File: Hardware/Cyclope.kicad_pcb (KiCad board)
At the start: 2 copper layers, 100 x 84 mm, 81 parts, among them J1 M20-9762042, J2 Motor_2, J3 Motor_1, J4 Front, J5 Front, J8 FTDI, M1 FS5113R, M2 FS5113R, Q1 DMG3414U, Q2 DMG2301L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

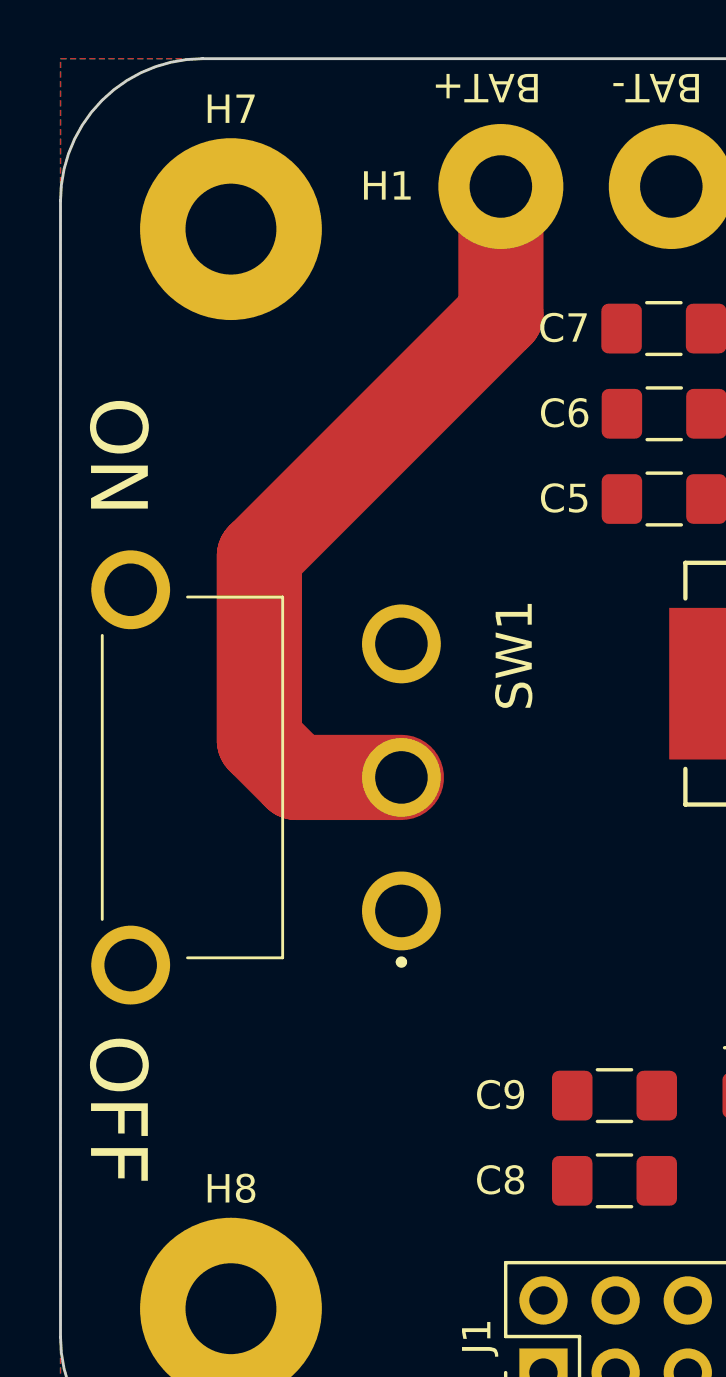
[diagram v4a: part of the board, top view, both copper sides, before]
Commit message: [Hardware] Changed power switch pins order to ease routing.
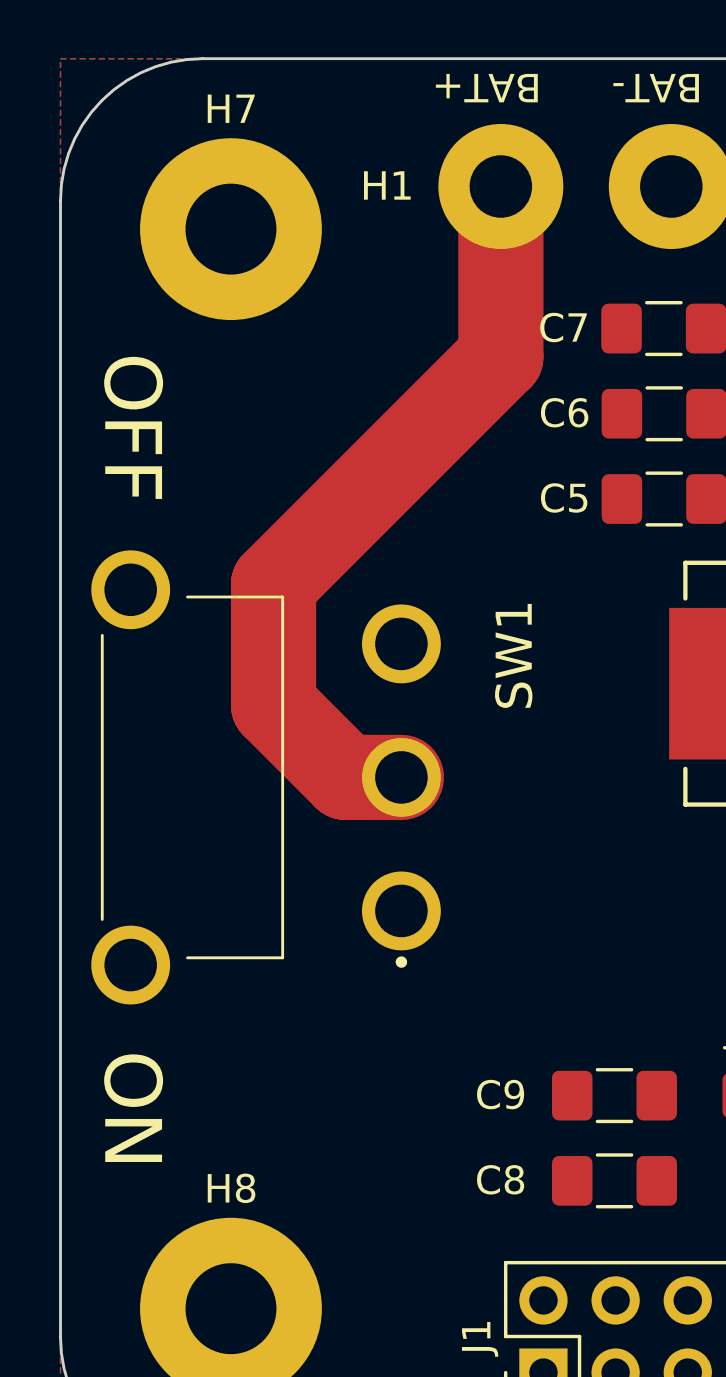
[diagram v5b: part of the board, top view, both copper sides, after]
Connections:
- SW1 pad 1: Net-(SW1-Pad1) -> BATTERY+
- SW1 pad 3: BATTERY+ -> Net-(SW1-Pad3)
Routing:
- net Net-(H1-Pad1): track 28.6 -> 27.1 mm

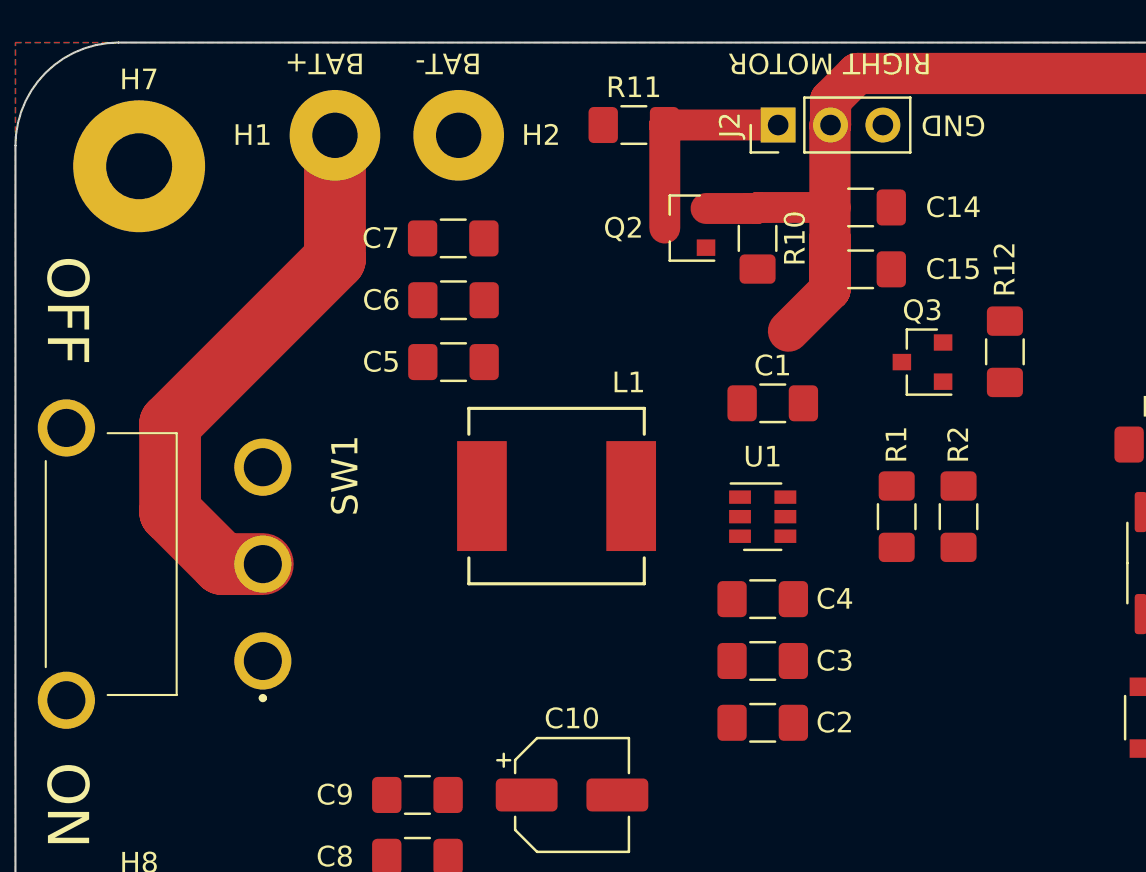
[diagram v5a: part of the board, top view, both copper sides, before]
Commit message: [Hardware] Routed motherboard DC/DC.
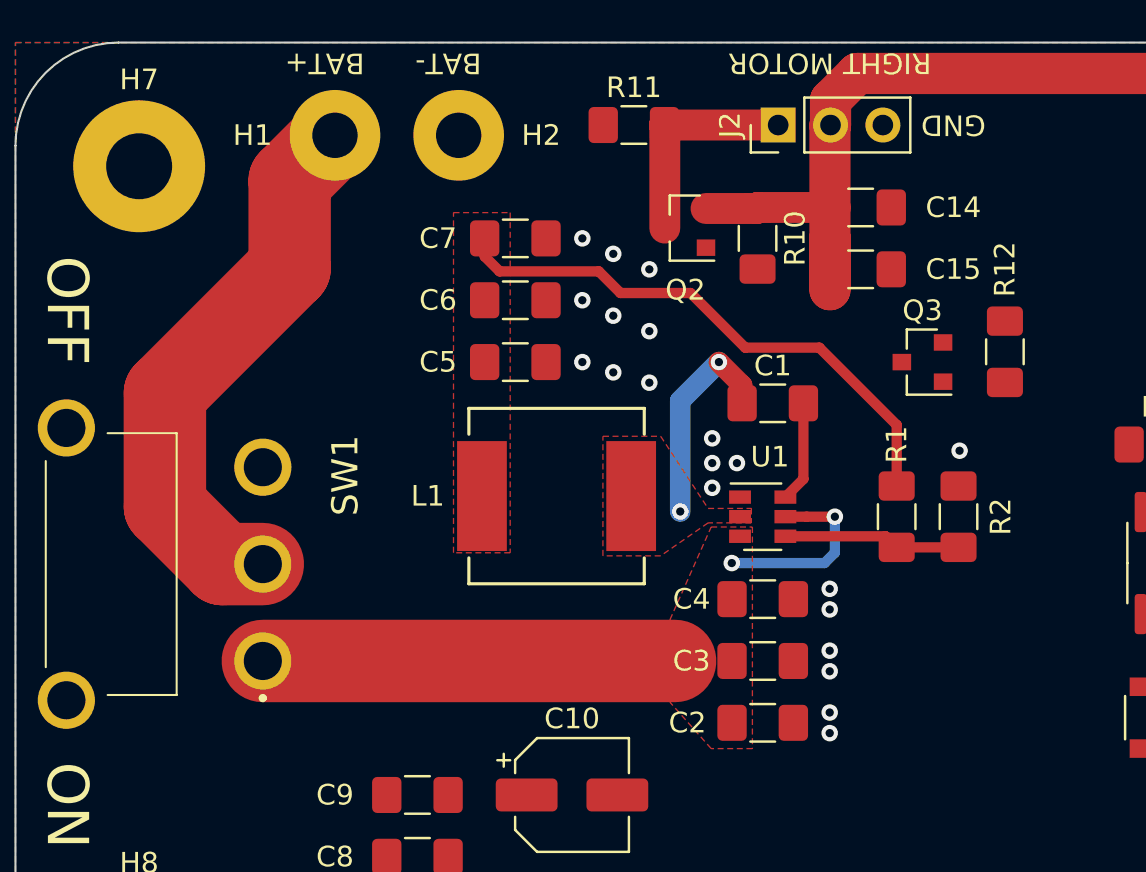
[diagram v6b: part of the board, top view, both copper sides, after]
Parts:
- moved C7 3.01 mm to (81.8, 69.5), turned to 180 degrees
- moved C5 3.00 mm to (81.8, 75.5), turned to 180 degrees
- moved C6 3.00 mm to (81.8, 72.5), turned to 180 degrees
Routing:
- net BATTERY+: track 0.00 -> 29.4 mm, vias 0 -> 2
- net +5V: track 76.6 -> 101.0 mm
- net Net-(C1-Pad1): track 0.00 -> 10.5 mm, vias 0 -> 2
- net Net-(R1-Pad2): track 0.00 -> 8.62 mm
- net Net-(C1-Pad2): track 0.00 -> 4.91 mm
- net GND: vias 0 -> 20
- added copper zone on F.Cu, net +5V
- added copper zone on F.Cu, net BATTERY+
- added copper zone on F.Cu, net Net-(C1-Pad1)

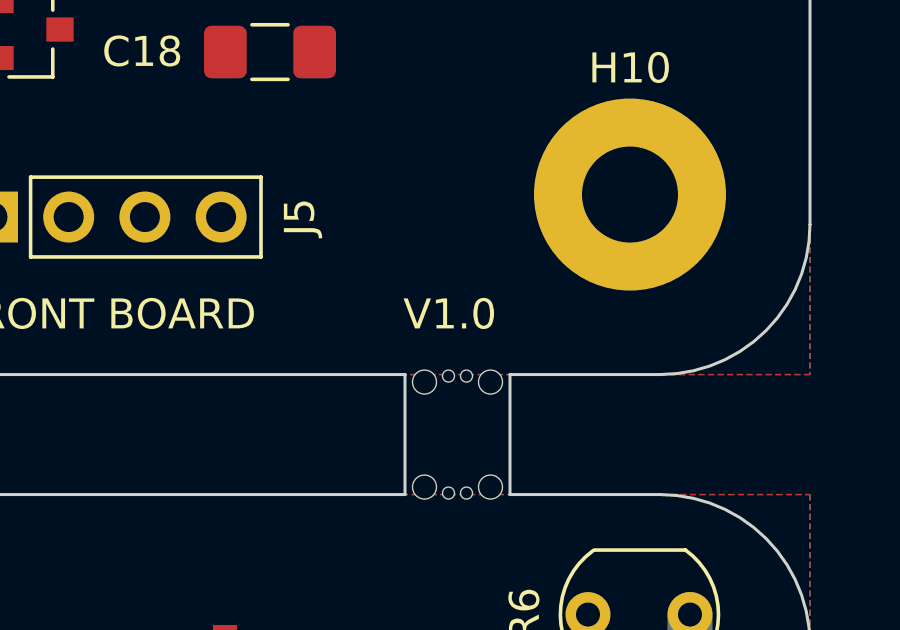
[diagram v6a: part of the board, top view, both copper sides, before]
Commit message: [Hardware] Added date marking to PCBs.
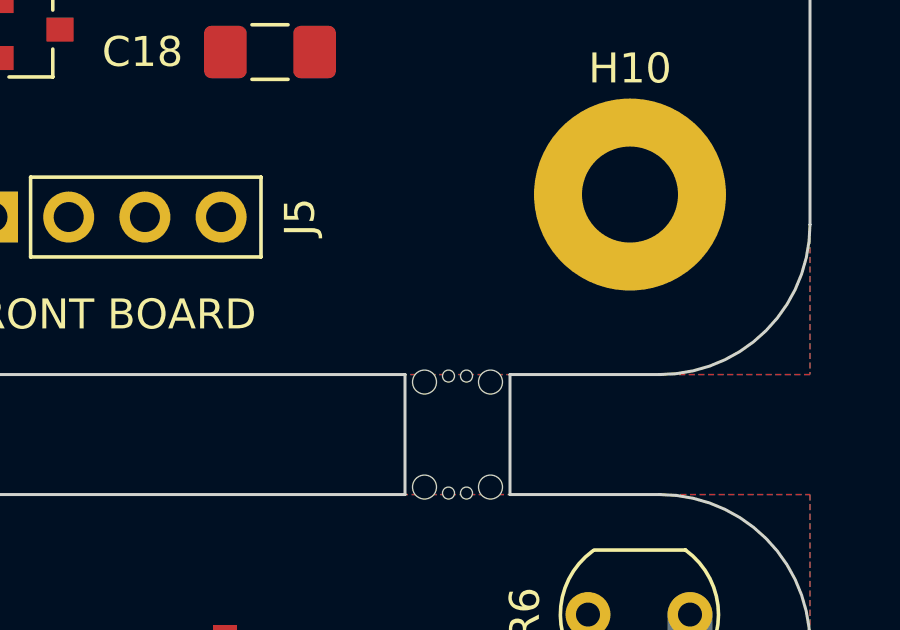
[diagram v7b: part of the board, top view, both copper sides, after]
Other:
- board text added: "14/08/2020"
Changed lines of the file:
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@@
   (general
     (thickness 1.6)
-    (drawings 64)
+    (drawings 66)
     (tracks 125)
     (zones 0)
@@
     )
   )
+  (gr_text 14/08/2020 (at 147.25 83.5 90) (layer F.Mask)
+    (effects (font (size 1 1) (thickness 0.15)))
+  )
+  (gr_text V1.0 (at 147.25 75.25 90) (layer F.Mask)
+    (effects (font (size 1 1) (thickness 0.15)))
+  )
+  (gr_text 14/08/2020 (at 133.25 142) (layer B.Mask)
+    (effects (font (size 1 1) (thickness 0.15)) (justify mirror))
+  )
   (gr_text GND (at 103 64 180) (layer F.SilkS)
     (effects (font (size 1 1) (thickness 0.15)))
@@
     (effects (font (size 1 1) (thickness 0.15)))
   )
-  (gr_text V1.0 (at 145.5 108) (layer F.SilkS)
-    (effects (font (size 1 1) (thickness 0.15)))
-  )
-  (gr_text V1.0 (at 141.5 142) (layer B.SilkS)
+  (gr_text V1.0 (at 141.5 142) (layer B.Mask)
     (effects (font (size 1 1) (thickness 0.15)) (justify mirror))
   )

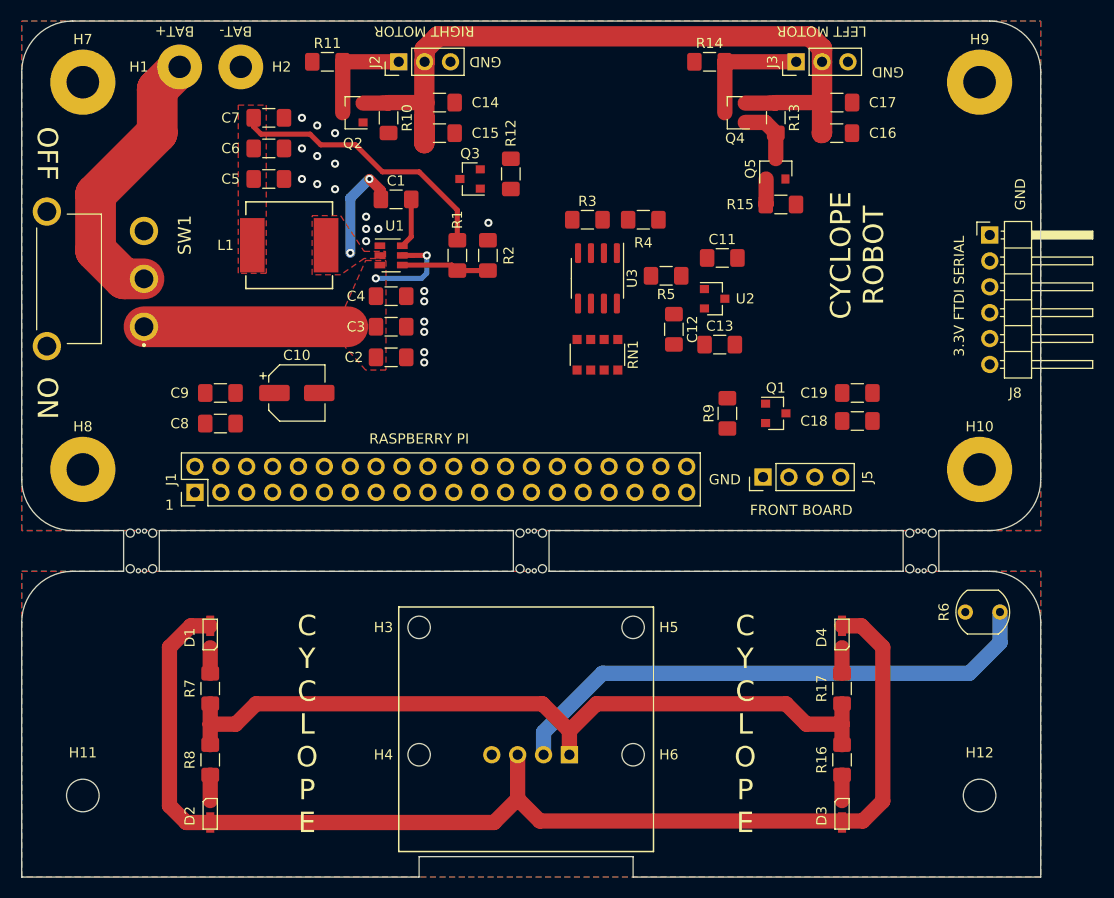
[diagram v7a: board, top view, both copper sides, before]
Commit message: [Hardware] Routed part of ADC, routed Raspberry Pi power supply.
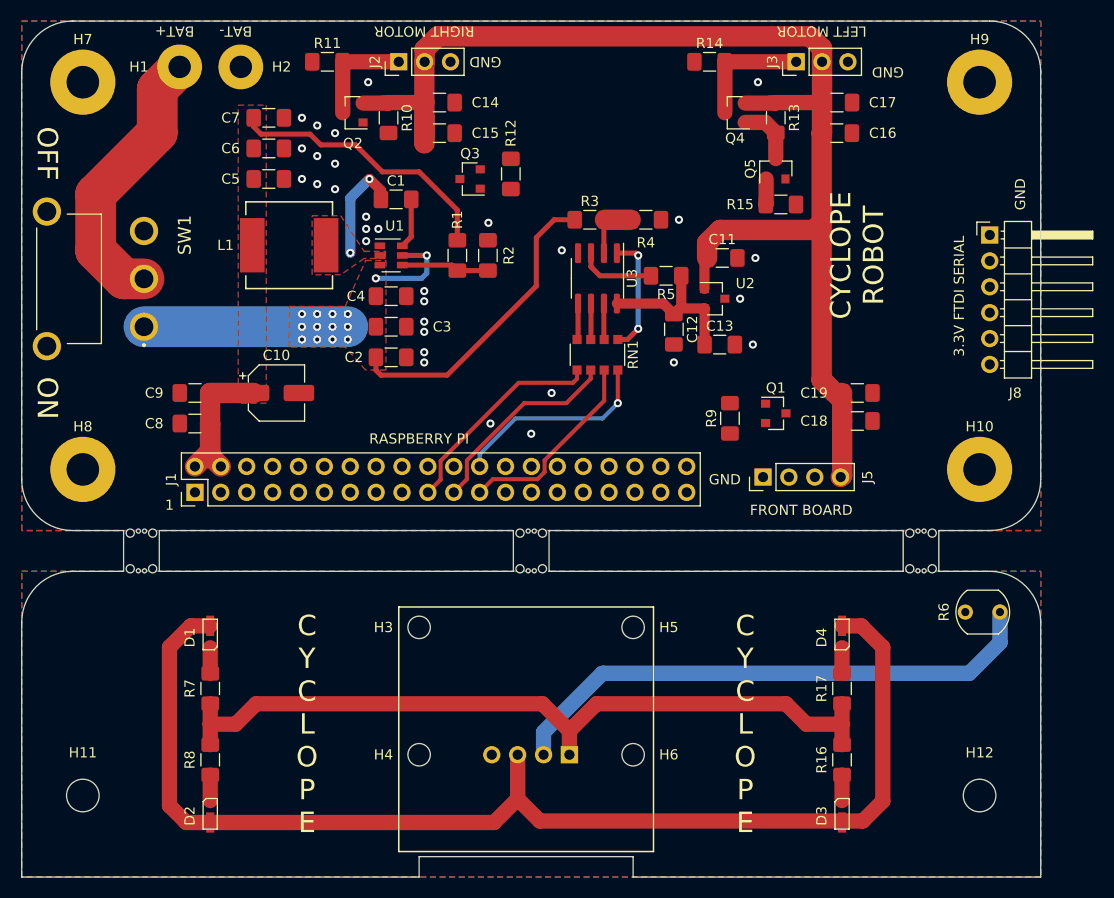
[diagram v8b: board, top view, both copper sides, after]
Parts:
- moved C8 2.50 mm to (74.5, 99.5)
- moved C9 2.50 mm to (74.5, 96.5)
- moved C10 2.00 mm to (82.5, 96.5)
- moved R9 0.55 mm to (127.0, 99.0)
- moved R4 0.25 mm to (118.8, 79.5)
- moved R3 0.24 mm to (113.2, 79.5)
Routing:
- net +5V: track 101.0 -> 171.7 mm
- net BATTERY+: track 29.4 -> 59.4 mm, vias 2 -> 14
- net ADC_SPI_MOSI: track 0.00 -> 21.2 mm
- net ADC_SPI_CS: track 0.00 -> 20.1 mm, vias 0 -> 1
- net ADC_SPI_MISO: track 0.00 -> 20.0 mm
- net ADC_SPI_SCK: track 0.00 -> 19.6 mm
- net +3.3VA: track 0.00 -> 16.9 mm
- net Net-(RN1-Pad1): track 0.00 -> 11.8 mm, vias 0 -> 2
- net FRONT_BOARD_LDR: track 0.00 -> 7.59 mm
- net Net-(R3-Pad2): track 0.00 -> 5.84 mm
- net Net-(RN1-Pad4): track 0.00 -> 3.56 mm
- net Net-(RN1-Pad3): track 0.00 -> 3.54 mm
- net Net-(RN1-Pad2): track 0.00 -> 3.54 mm
- net GND: vias 20 -> 31
